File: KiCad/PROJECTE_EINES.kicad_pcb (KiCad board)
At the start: 2 copper layers, 107 x 101.9 mm, 63 parts, among them J1 DE9_Pins_MountingHoles, J2 DE9_Pins_MountingHoles, J3 Conn_01x08_Pin, SW1 SS-1GL2-F-D, SW2 SW_DPDT_x2, SW3 SW_DPDT_x2, SW4 SW_DPDT_x2, U1 PIC24HJ128GP504-I_PT, U2 SN65HVD230, U3 VNH5019A-E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

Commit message: V1 Routing
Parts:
- removed C16: 100n, Capacitor_SMD:C_0805_2012Metric
- removed C2: 100nF, Capacitor_SMD:C_0805_2012Metric
- removed the CIN1 at (118.3, 42.5)
- removed C_VDD2: 100nF, Capacitor_SMD:C_0603_1608Metric
- removed R4: 10k, Resistor_SMD:R_0805_2012Metric
- removed SW4: SW_DPDT_x2, Button_Switch_SMD:SW_DPDT_CK_JS202011JCQN
- added REF**: MountingHole_3.2mm_M3, MountingHole:MountingHole_3.2mm_M3, F.Cu at (88.5, 100.2)
- added REF**: MountingHole_3.2mm_M3, MountingHole:MountingHole_3.2mm_M3, F.Cu at (197.0, 100.7)
- added REF**: MountingHole_3.2mm_M3, MountingHole:MountingHole_3.2mm_M3, F.Cu at (197.3, 27.9)
- added REF**: MountingHole_3.2mm_M3, MountingHole:MountingHole_3.2mm_M3, F.Cu at (88.2, 27.7)
- C3, C_VCAP1: moved to F.Cu
- C_AVDD1, C_VDD1: footprint Capacitor_SMD:C_0603_1608Metric -> Capacitor_SMD:C_0805_2012Metric; moved to F.Cu
- J1, J2: footprint Connector_Dsub:DSUB-15_Socket_Horizontal_P2.77x2.84mm_EdgePinOffset4.94mm_Housed_MountingHolesOffset4.94mm -> Connector_Dsub:DSUB-9_Pins_Horizontal_P2.77x2.84mm_EdgePinOffset4.94mm_Housed_MountingHolesOffset4.94mm
- SW1: value SS-1GL2-F-D -> SW_DPDT_x2; footprint Connector_PinSocket_1.00mm:PinSocket_1x03_P1.00mm_Vertical -> Button_Switch_SMD:SW_DPDT_CK_JS202011JCQN
- SW2: footprint Button_Switch_SMD:SW_DPDT_CK_JS202011JCQN -> Button_Switch_THT:SW_CK_JS202011CQN_DPDT_Straight
- SW3: footprint Button_Switch_SMD:SW_DPDT_CK_JS202011JCQN -> TerminalBlock:TerminalBlock_MaiXu_MX126-5.0-02P_1x02_P5.00mm
- moved J_DEBUG1 110.5 mm to (159.1, 34.7), turned to -90 degrees
- moved J3 110.4 mm to (173.9, 33.9)
- moved SW_UP1 89.9 mm to (167.1, 36.0), turned to 180 degrees
- moved R_MCLR1 87.9 mm to (164.1, 41.6), turned to 180 degrees
- moved SW1 81.4 mm to (167.0, 93.0)
- moved C3 67.8 mm to (181.9, 36.6), turned to 0 degrees
- moved R_Lock/Unlock1 61.4 mm to (177.4, 88.4)
- moved R1 55.9 mm to (138.9, 93.4)
- moved C_BULK1 54.6 mm to (159.3, 75.7), turned to -90 degrees
- moved C_WIN_CP1 53.6 mm to (127.7, 58.3)
- moved R_WIN_CS1 53.2 mm to (127.8, 67.2)
- moved R_WIN_DIAGA1 53.2 mm to (128.0, 71.5)
- moved R_WIN_DIAGB1 53.2 mm to (127.8, 62.8)
- moved J_MOTOR_WIN1 53.1 mm to (94.2, 62.5)
- moved U3 52.1 mm to (114.1, 65.1)
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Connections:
- J3 pad 1: RFID_CS -> RFID_MOSI
- J3 pad 2: RFID_SCK -> RFID_MISO
- J3 pad 3: RFID_MOSI -> RFID_CS
- J3 pad 4: RFID_MISO -> RFID_RST
- J3 pad 5: RFID_RST -> RFID_SCK
- J_DEBUG1 pad 1: MCLR -> GND
- J_DEBUG1 pad 3: GND -> MCLR
- R_Lock/Unlock1 pad 2: Net-(SW4A-B) -> Net-(SW2A-B)
- SW1 pad 1: GND -> WIN_BTN_UP
- SW1 pad 2: unconnected-(SW1-NC-Pad2) -> GND
- SW1 pad 3: WIN_CURRENT_ADC -> WIN_BTN_DOWN
- SW2 pad 1: WIN_BTN_UP -> +3.3V
- SW2 pad 2: GND -> Net-(SW2A-B)
- SW2 pad 3: WIN_BTN_DOWN -> GND
- U1 pad 1: WIN_LIMIT -> unconnected-(U1-SDA1/RP9(1)/CN21/PMD3/RB9-Pad1)
- U1 pad 10: WIN_INB -> unconnected-(U1-AN12/RP12(1)/CN14/PMD0/RB12-Pad10)
- U1 pad 11: WIN_CURRENT_ADC -> RFID_SCK
- U1 pad 12: DOOR_LOCK/UNLOCK -> RFID_RST
- U1 pad 13: unconnected-(U1-TCK/PMA7/RA7-Pad13) -> RFID_CS
- U1 pad 14: WIN_DIAGA -> RFID_MISO
- U1 pad 15: WIN_DIAGB -> RFID_MOSI
- U1 pad 19: RFID_CS -> unconnected-(U1-AN0/VREF+/CN2/RA0-Pad19)
- U1 pad 2: DOOR_DIAGA -> UART_RX
- U1 pad 23: UART_TX -> WIN_INB
- U1 pad 24: UART_RX -> WIN_DIAGB
- U1 pad 25: DOOR_PWM -> WIN_CURRENT_ADC
- U1 pad 26: DOOR_INA -> WIN_PWM
- U1 pad 27: DOOR_INB -> WIN_DIAGA
- U1 pad 3: DOOR_DIAGB -> UART_TX
- U1 pad 32: unconnected-(U1-TDO/PMA8/RA8-Pad32) -> WIN_INA
- U1 pad 33: RFID_MISO -> DOOR_INB
- U1 pad 34: RFID_RST -> DOOR_DIAGB
- U1 pad 36: unconnected-(U1-RP19(1)/CN28/PMBE/RC3-Pad36) -> DOOR_PWM
- U1 pad 37: CAN_RX -> DOOR_DIAGA
- U1 pad 38: CAN_TX -> DOOR_INA
- U1 pad 4: unconnected-(U1-RP24(1)/CN20/PMA5/RC8-Pad4) -> CAN_RX
- U1 pad 41: RFID_MOSI -> WIN_LIMIT
- U1 pad 42: RFID_SCK -> WIN_BTN_UP
- U1 pad 43: WIN_BTN_UP -> WIN_BTN_DOWN
- U1 pad 44: WIN_BTN_DOWN -> DOOR_LOCK/UNLOCK
- U1 pad 5: unconnected-(U1-RP25(1)/CN19/PMA6/RC9-Pad5) -> CAN_TX
- U1 pad 8: WIN_PWM -> unconnected-(U1-PGED2/EMCD2/RP10(1)/CN16/PMD2/RB10-Pad8)
- U1 pad 9: WIN_INA -> unconnected-(U1-PGEC2/RP11(1)/CN15/PMD1/RB11-Pad9)
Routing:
- net +3.3V: track 0.00 -> 131.2 mm, vias 0 -> 9
- net GNDPWR: track 0.00 -> 114.1 mm, vias 0 -> 30
- net GND: track 0.00 -> 67.5 mm, vias 0 -> 29
- net MCLR: track 0.00 -> 43.7 mm
- net DOOR_INA: track 0.00 -> 43.4 mm
- net DOOR_DIAGA: track 0.00 -> 42.5 mm
- net DOOR_PWM: track 0.00 -> 39.9 mm
- net +5V: track 0.00 -> 38.0 mm
- net DOOR_INB: track 0.00 -> 35.6 mm
- net RFID_SCK: track 0.00 -> 35.5 mm
- net DOOR_MOTOR_B: track 0.00 -> 34.4 mm
- net WIN_MOTOR_B: track 0.00 -> 34.0 mm
- net WIN_MOTOR_A: track 0.00 -> 33.9 mm
- net DOOR_MOTOR_A: track 0.00 -> 33.7 mm
- net WIN_INA: track 0.00 -> 33.6 mm
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- added copper zone on F.Cu, net +3.3V
- added copper zone on B.Cu, net GND
- added copper zone on B.Cu, net GNDPWR
- added copper zone on F.Cu, net VBAT_PROT
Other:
- board size 107 x 101.9 mm -> 117.7 x 80.6 mm

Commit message: V2 Routing
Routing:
- net GNDPWR: track 114.1 -> 116.7 mm
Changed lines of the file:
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@@
+	)
+	(segment
+		(start 131.7201 68.5001)
+		(end 128.1808 68.5001)
+		(width 2)
+		(layer "F.Cu")
+		(net 3)
 	)
 	(segment
@@
 	)
 	(segment
-		(start 129.57 69.19)
-		(end 128.8801 68.5001)
-		(width 2)
-		(layer "F.Cu")
-		(net 3)
-	)
-	(segment
 		(start 104.94 83.075)
 		(end 104.94 82.656)
@@
 	)
 	(segment
+		(start 132.21 68.99)
+		(end 131.7201 68.5001)
+		(width 2)
+		(layer "F.Cu")
+		(net 3)
+	)
+	(segment
 		(start 125.94 51.75)
 		(end 123.94 51.75)
@@
 	)
 	(segment
-		(start 128.8801 68.5001)
-		(end 128.1808 68.5001)
-		(width 2)
-		(layer "F.Cu")
-		(net 3)
-	)
-	(segment
 		(start 125.94 51.75)
 		(end 125.94 53.22)
@@
 	)
 	(via
-		(at 129.57 69.19)
+		(at 132.21 68.99)
 		(size 0.6)
 		(drill 0.3)
@@
 		(net 7)
 	)
-	(segment
-		(start 134.4665 79.04)
-		(end 134.4865 79.06)
-		(width 0.2)
-		(layer "B.Cu")
-		(net 7)
-	)

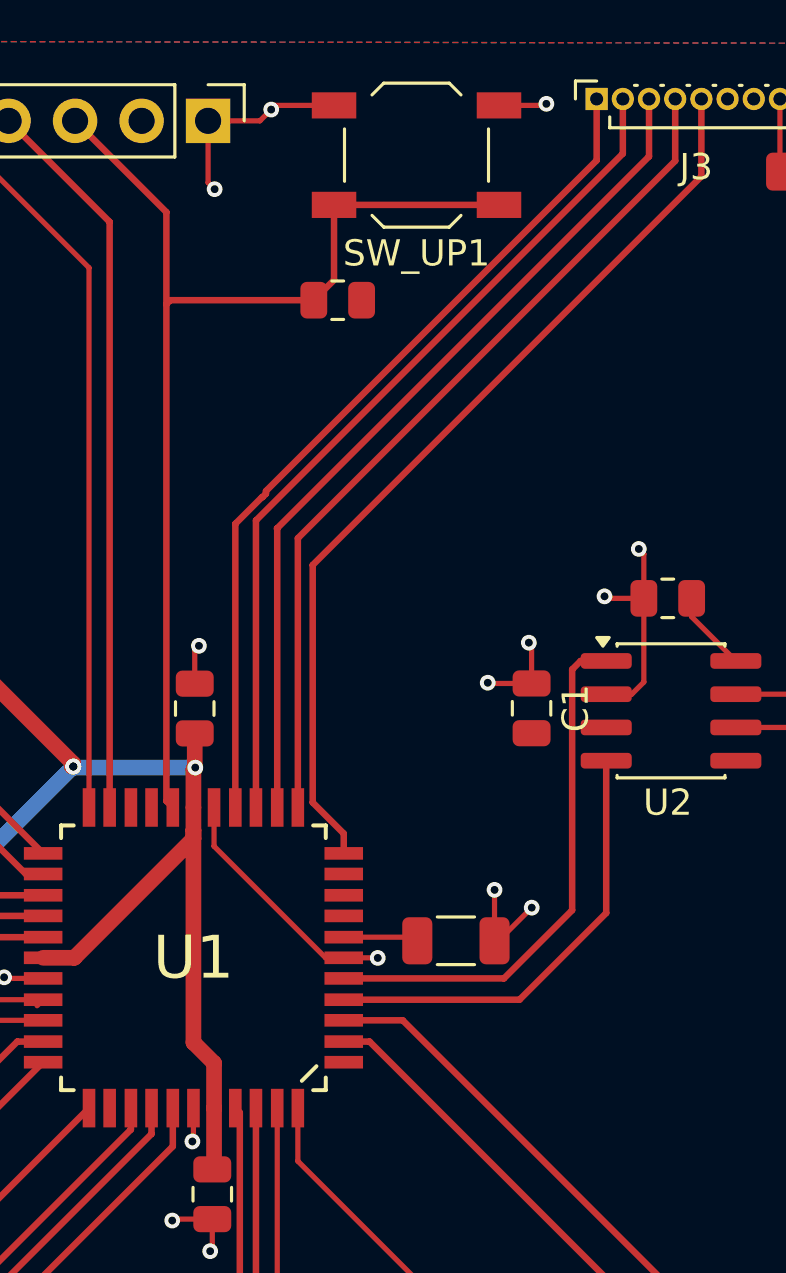
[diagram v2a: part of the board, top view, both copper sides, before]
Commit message: Update dels testpins
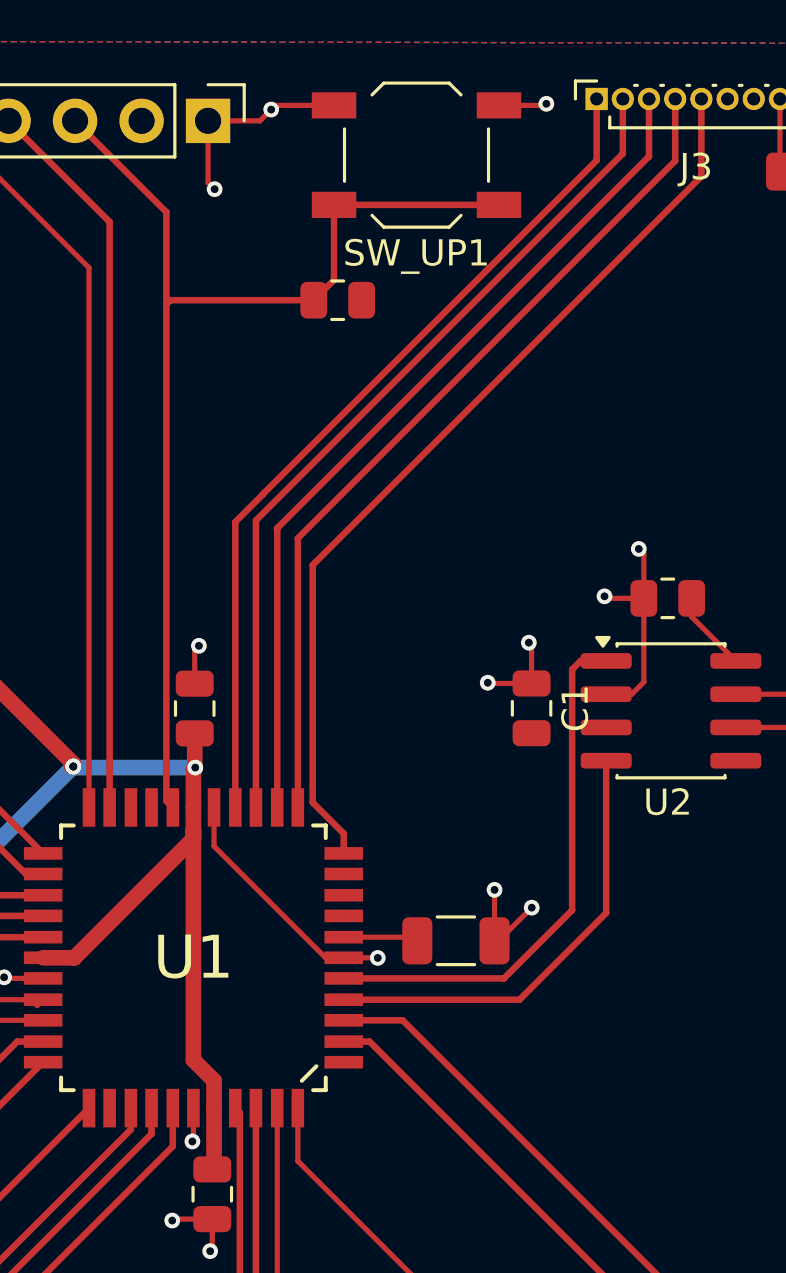
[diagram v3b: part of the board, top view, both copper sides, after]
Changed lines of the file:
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@@
-	)
-	(segment
-		(start 158.54 69.91)
-		(end 159.3274 70.6974)
-		(width 0.6)
-		(layer "F.Cu")
-		(net 2)
 	)
 	(segment
@@
 	)
 	(segment
+		(start 158.54 61.8)
+		(end 158.54 70.58)
+		(width 0.6)
+		(layer "F.Cu")
+		(net 2)
+	)
+	(segment
 		(start 129.8032 72.4532)
 		(end 130 72.65)
@@
 	)
 	(segment
-		(start 158.54 61.8)
-		(end 158.54 69.91)
-		(width 0.6)
-		(layer "F.Cu")
-		(net 2)
-	)
-	(segment
 		(start 125.215 49.525)
 		(end 125.94 48.8)
@@
 	)
 	(segment
+		(start 159.3274 71.3674)
+		(end 159.3274 72.4154)
+		(width 0.6)
+		(layer "F.Cu")
+		(net 2)
+	)
+	(segment
 		(start 144.6937 50.0025)
 		(end 153.9512 59.26)
@@
 	)
 	(segment
-		(start 159.3274 70.6974)
-		(end 159.3274 72.4154)
-		(width 0.6)
-		(layer "F.Cu")
-		(net 2)
-	)
-	(segment
 		(start 127.7651 63.7429)
 		(end 130.0071 63.7429)
@@
 	)
 	(segment
+		(start 158.54 70.58)
+		(end 159.3274 71.3674)
+		(width 0.6)
+		(layer "F.Cu")
+		(net 2)
+	)
+	(segment
 		(start 158.54 60.9346)
 		(end 158.54 59.48)
@@
 	)
 	(segment
-		(start 160.1402 50.1002)
-		(end 160.1402 60.9346)
-		(width 0.25)
-		(layer "F.Cu")
-		(net 23)
-	)
-	(segment
-		(start 161.31 48.95219)
-		(end 161.18219 49.08)
-		(width 0.25)
-		(layer "F.Cu")
-		(net 23)
-	)
-	(segment
-		(start 161.31 48.85)
-		(end 161.31 48.95219)
-		(width 0.25)
-		(layer "F.Cu")
-		(net 23)
-	)
-	(segment
-		(start 173.94 36.22)
-		(end 161.31 48.85)
-		(width 0.25)
-		(layer "F.Cu")
-		(net 23)
-	)
-	(segment
-		(start 161.1604 49.08)
-		(end 160.1402 50.1002)
-		(width 0.25)
-		(layer "F.Cu")
-		(net 23)
-	)
-	(segment
 		(start 173.94 33.875)
 		(end 173.94 36.22)
@@
 	)
 	(segment
-		(start 161.18219 49.08)
-		(end 161.1604 49.08)
-		(width 0.25)
-		(layer "F.Cu")
+		(start 160.1402 50.0298)
+		(end 160.1402 60.9346)
+		(width 0.25)
+		(layer "F.Cu")
+		(net 23)
+	)
+	(segment
+		(start 173.94 36.22)
+		(end 161.2 48.96)
+		(width 0.25)
+		(layer "F.Cu")
+		(net 23)
+	)
+	(segment
+		(start 161.2 48.96)
+		(end 161.2 48.97)
+		(width 0.25)
+		(layer "F.Cu")
+		(net 23)
+	)
+	(segment
+		(start 161.2 48.97)
+		(end 160.1402 50.0298)
+		(width 0.25)
+		(layer "F.Cu")

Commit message: Routing V3
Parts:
- moved R_WIN_DIAGB1 9.60 mm to (137.1, 65.0)
- moved R_WIN_DIAGA1 9.52 mm to (137.0, 74.6)
- moved R_DIAGA_DOOR1 8.14 mm to (136.6, 88.0)
- moved R1 7.80 mm to (133.7, 99.3)
- moved R_DIAGB_DOOR1 7.48 mm to (136.7, 82.7)
- moved C_WIN_CP1 1.47 mm to (128.0, 59.7), turned to 180 degrees
- moved R_CS_DOOR1 0.83 mm to (128.4, 87.2), turned to 0 degrees
- moved R_MCLR1 0.72 mm to (164.7, 41.3)
- moved C_CP_DOOR1 0.62 mm to (128.8, 78.9), turned to 180 degrees
- moved C_AVDD1 0.55 mm to (159.1, 57.1)
- moved C_OSC2 0.23 mm to (142.6, 69.9)
- moved C_OSC1 0.23 mm to (142.6, 67.7)
- moved Y1 0.23 mm to (146.8, 68.8)
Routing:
- net +3.3V: track 131.2 -> 16.8 mm, vias 9 -> 7
- net GND: track 67.4 -> 0.00 mm, vias 29 -> 52
- net GNDPWR: track 116.7 -> 71.5 mm, vias 30 -> 28
- net DOOR_INA: track 43.4 -> 0.00 mm
- net DOOR_DIAGA: track 42.5 -> 0.00 mm
- net RFID_SCK: track 35.5 -> 0.00 mm
- net UART_RX: track 28.0 -> 0.00 mm
- net UART_TX: track 27.2 -> 0.00 mm
- net WIN_BTN_DOWN: track 24.9 -> 0.00 mm
- net WIN_LIMIT: track 21.7 -> 0.00 mm
- net DOOR_LOCK/UNLOCK: track 21.7 -> 0.00 mm
- net WIN_BTN_UP: track 20.9 -> 0.00 mm
- net CAN_TX: track 20.4 -> 0.00 mm
- net CAN_RX: track 17.2 -> 0.00 mm
- net /COMUNICACIONS/CANH: track 14.5 -> 0.00 mm
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- added copper zone on F.Cu, net GND

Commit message: Versió preliminar Routing Final
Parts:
- removed C_VDD1: 100nF, Capacitor_SMD:C_0805_2012Metric
- added C_VDD2: 100nF, Capacitor_SMD:C_0805_2012Metric, F.Cu at (145.2, 62.6)
- C_VCAP1: footprint Capacitor_SMD:C_1206_3216Metric -> Capacitor_SMD:C_0805_2012Metric
- moved R3 8.78 mm to (186.7, 50.2)
- moved R2 8.36 mm to (180.6, 45.6)
- moved U2 7.44 mm to (179.0, 50.1)
- moved C1 7.25 mm to (173.0, 50.1)
- moved J1 6.78 mm to (193.5, 54.0)
- moved J2 6.74 mm to (193.4, 86.2)
- moved R1 5.80 mm to (134.8, 93.6)
- moved C_BULK1 1.55 mm to (158.8, 77.2)
- moved C_OSC1 1.01 mm to (143.6, 67.7)
- moved C_OSC2 0.96 mm to (143.6, 69.9)
- moved Y1 0.96 mm to (147.7, 68.8)
- moved C_VCAP1 0.20 mm to (168.4, 65.9)
- moved R_Lock/Unlock1 0.17 mm to (177.5, 88.3)
- turned C_INBUCK2 to 180 degrees
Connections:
- net Net-(U1-OSC1/CLKI/CN30/RA2) renamed OSC_+
- net Net-(U1-OSC2/CLKO/CN29/RA3) renamed OSC_-
- U1 pad 10: unconnected-(U1-AN12/RP12(1)/CN14/PMD0/RB12-Pad10) -> CAN_TX
- U1 pad 4: CAN_RX -> unconnected-(U1-RP24(1)/CN20/PMA5/RC8-Pad4)
- U1 pad 5: CAN_TX -> unconnected-(U1-RP25(1)/CN19/PMA6/RC9-Pad5)
- U1 pad 9: unconnected-(U1-PGEC2/RP11(1)/CN15/PMD1/RB11-Pad9) -> CAN_RX
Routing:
- net +3.3V: track 16.8 -> 259.8 mm, vias 7 -> 9
- net GND: track 0.00 -> 69.3 mm, vias 52 -> 31
- net GNDPWR: track 71.5 -> 139.0 mm, vias 28 -> 35
- net DOOR_INA: track 0.00 -> 43.7 mm
- net DOOR_DIAGA: track 0.00 -> 42.0 mm
- net RFID_SCK: track 0.00 -> 35.9 mm
- net UART_RX: track 0.00 -> 34.8 mm
- net UART_TX: track 0.00 -> 33.9 mm
- net CAN_TX: track 0.00 -> 24.1 mm
- net DOOR_LOCK/UNLOCK: track 0.00 -> 23.6 mm
- net WIN_BTN_DOWN: track 0.00 -> 22.7 mm
- net WIN_LIMIT: track 0.00 -> 21.6 mm
- net WIN_BTN_UP: track 0.00 -> 20.9 mm
- net CAN_RX: track 0.00 -> 18.7 mm
- net /COMUNICACIONS/CANH: track 0.00 -> 15.2 mm
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- removed copper zone on F.Cu, net GND

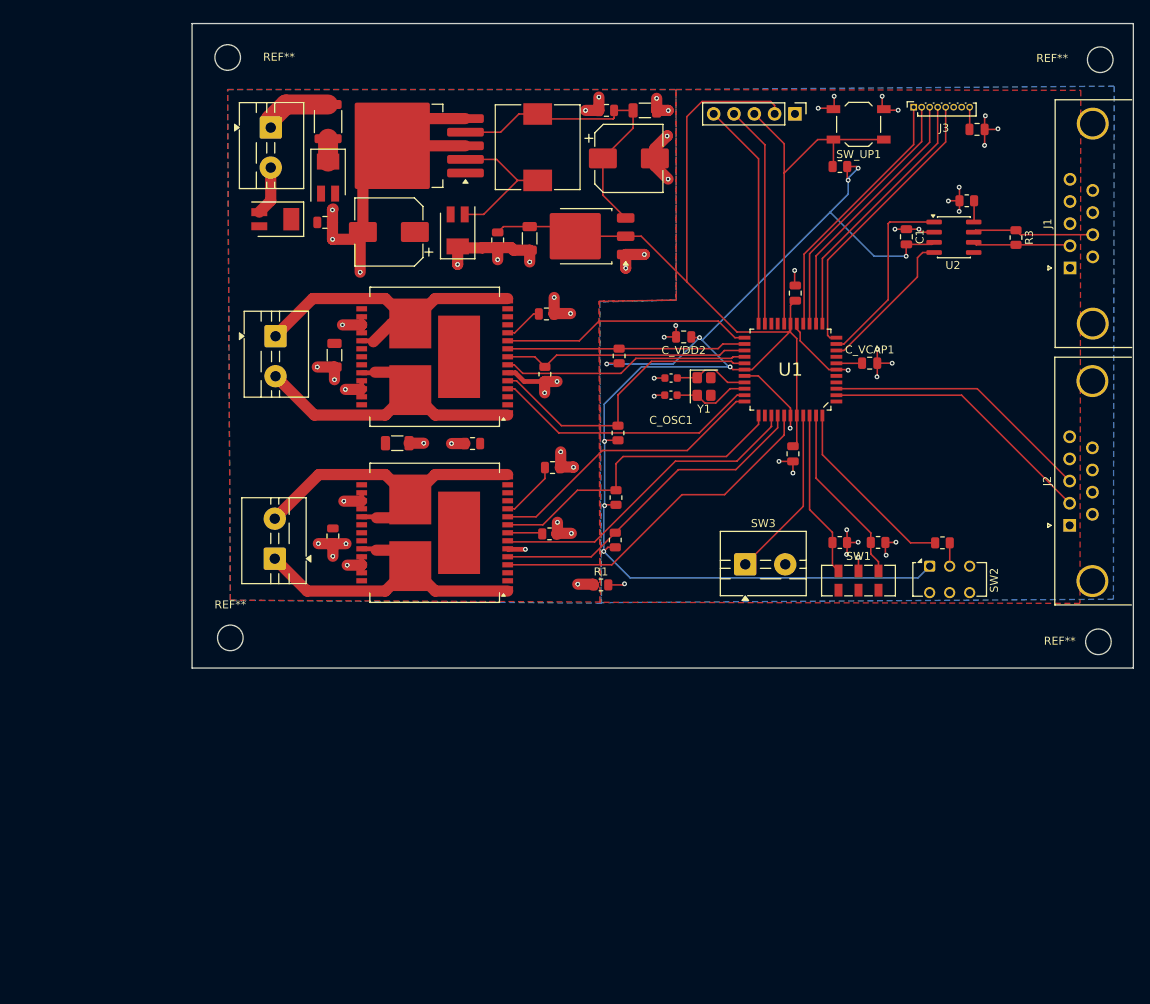
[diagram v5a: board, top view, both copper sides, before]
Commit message: Actualització dels test points
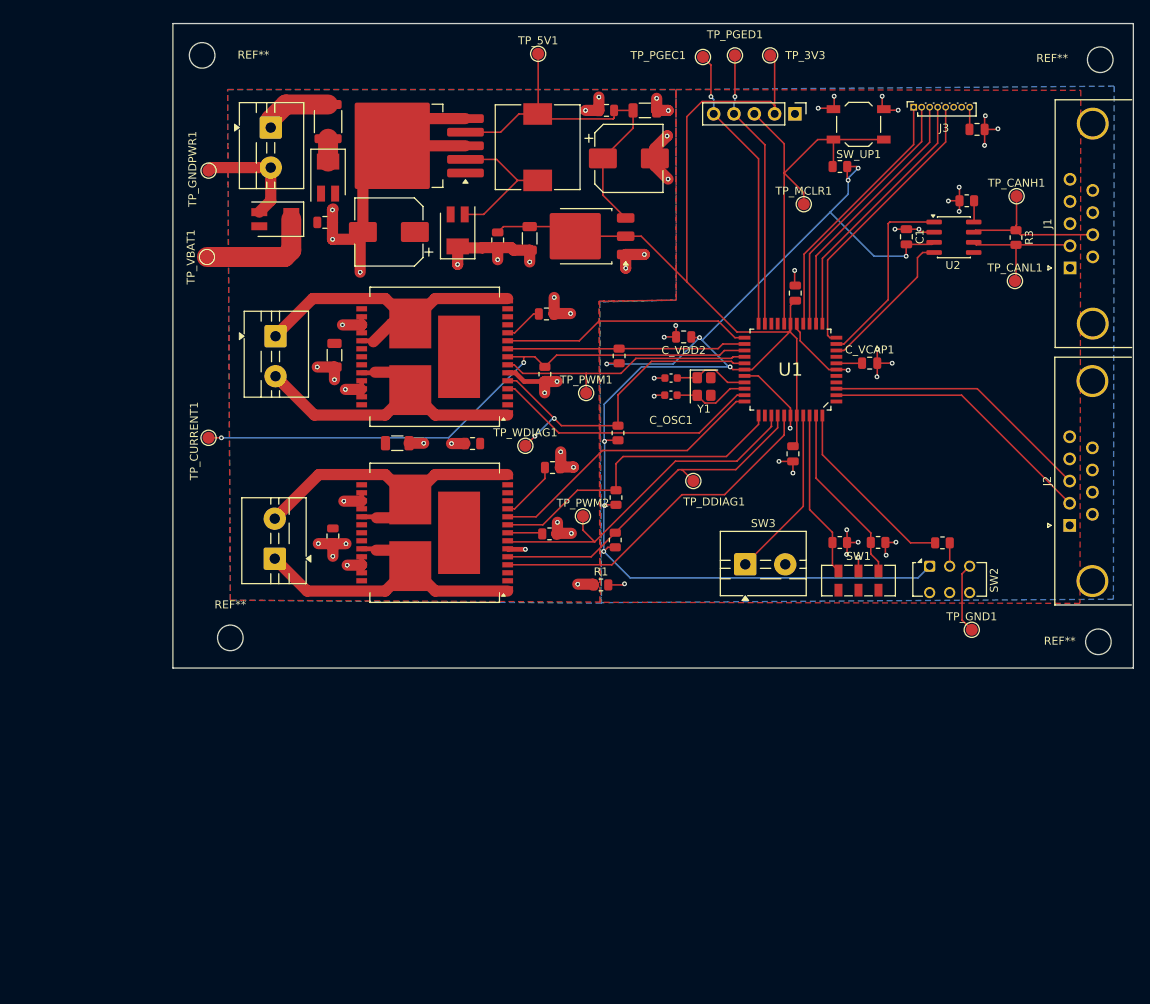
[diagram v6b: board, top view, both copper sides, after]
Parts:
- added TP_3V3: TestPoint, TestPoint:TestPoint_Pad_D1.5mm, F.Cu at (156.0, 27.4)
- added TP_5V1: TestPoint, TestPoint:TestPoint_Pad_D1.5mm, F.Cu at (127.0, 27.2)
- added TP_CANH1: ~, TestPoint:TestPoint_Pad_D1.5mm, F.Cu at (186.8, 45.0)
- added TP_CANL1: ~, TestPoint:TestPoint_Pad_D1.5mm, F.Cu at (186.6, 55.6)
- added TP_CURRENT1: ~, TestPoint:TestPoint_Pad_D1.5mm, F.Cu at (85.8, 75.2)
- added TP_DDIAG1: ~, TestPoint:TestPoint_Pad_D1.5mm, F.Cu at (146.4, 80.6)
- added TP_GND1: TestPoint, TestPoint:TestPoint_Pad_D1.5mm, F.Cu at (181.2, 99.2)
- added TP_GNDPWR1: TestPoint, TestPoint:TestPoint_Pad_D1.5mm, F.Cu at (85.8, 41.8)
- added TP_MCLR1: ~, TestPoint:TestPoint_Pad_D1.5mm, F.Cu at (160.2, 46.0)
- added TP_PGEC1: ~, TestPoint:TestPoint_Pad_D1.5mm, F.Cu at (147.6, 27.6)
- added TP_PGED1: ~, TestPoint:TestPoint_Pad_D1.5mm, F.Cu at (151.6, 27.4)
- added TP_PWM1: ~, TestPoint:TestPoint_Pad_D1.5mm, F.Cu at (133.0, 69.6)
- added TP_PWM2: ~, TestPoint:TestPoint_Pad_D1.5mm, F.Cu at (132.6, 85.0)
- added TP_VBAT1: TestPoint, TestPoint:TestPoint_Pad_D1.5mm, F.Cu at (85.6, 52.6)
- added TP_WDIAG1: ~, TestPoint:TestPoint_Pad_D1.5mm, F.Cu at (125.4, 76.2)
- moved REF** 3.20 mm to (85.0, 27.4)
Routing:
- net WIN_CURRENT_ADC: track 31.0 -> 75.0 mm, vias 0 -> 2
- net VBAT_PROT: track 0.77 -> 15.6 mm
- net GND: track 69.3 -> 78.2 mm
- net GNDPWR: track 139.0 -> 146.9 mm
- net PGEC1: track 28.5 -> 36.2 mm, vias 0 -> 1
- net +5V: track 39.3 -> 46.9 mm
- net +3.3V: track 259.8 -> 267.4 mm
- net PGED1: track 27.8 -> 35.2 mm, vias 0 -> 1
- net WIN_DIAGA: track 37.6 -> 42.7 mm, vias 0 -> 2
- net MCLR: track 45.4 -> 50.3 mm
- net /COMUNICACIONS/CANL: track 12.2 -> 16.8 mm
- net /COMUNICACIONS/CANH: track 15.2 -> 19.5 mm
- net DOOR_PWM: track 40.4 -> 44.2 mm
- net WIN_PWM: track 30.9 -> 33.4 mm
- net DOOR_DIAGA: track 42.0 -> 44.0 mm
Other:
- board size 117.7 x 80.6 mm -> 120.1 x 80.6 mm
